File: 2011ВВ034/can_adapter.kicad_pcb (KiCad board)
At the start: 2 copper layers, 31 x 12 mm, 8 parts

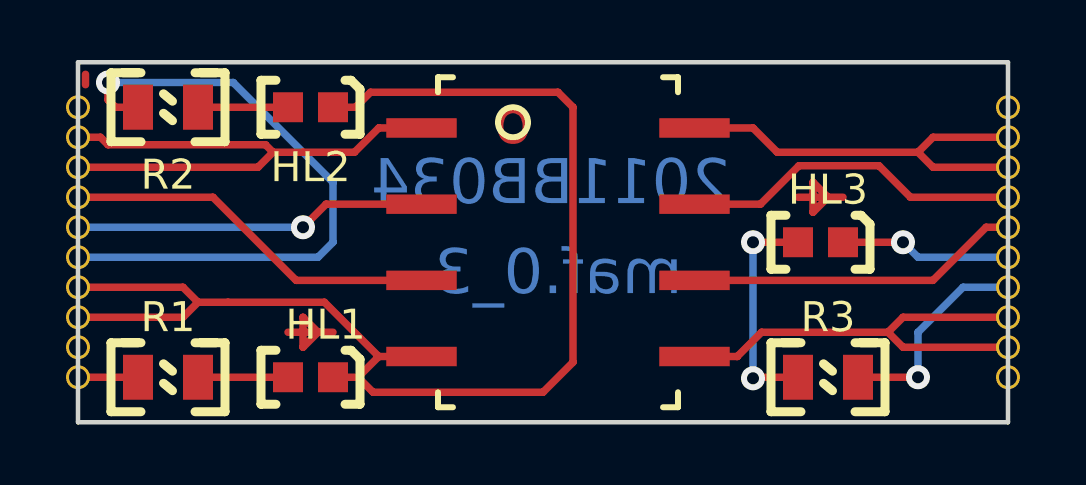
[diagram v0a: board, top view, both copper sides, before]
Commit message: увеличены зазоры и квадратизированы площадки
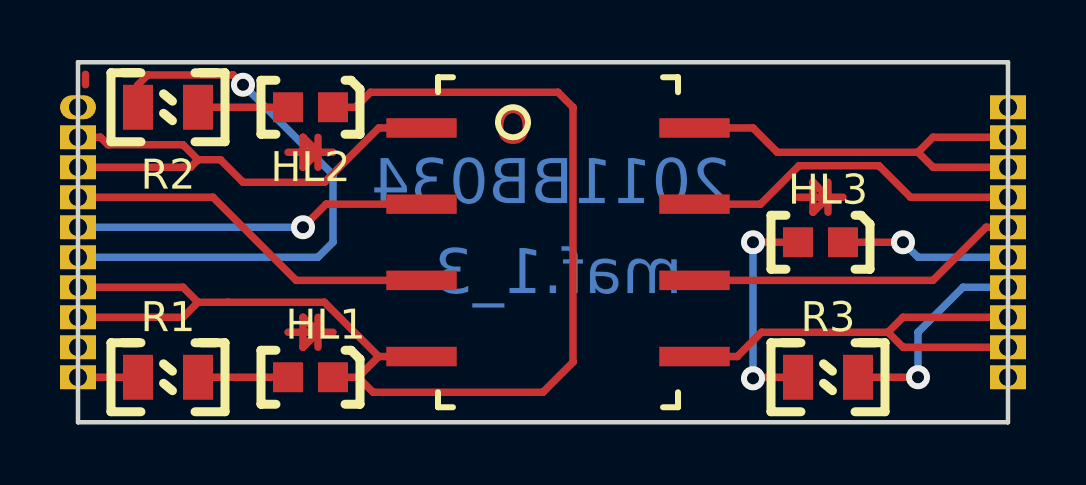
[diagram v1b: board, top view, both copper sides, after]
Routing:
- net (no net): track 8.18 -> 15.1 mm
- net Net-(A1-Pad2A): track 18.7 -> 16.9 mm
- net Net-(A1-Pad6A): track 21.3 -> 19.7 mm
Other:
- board text added: "maf.1_3"
- board text removed: "maf.0_3"
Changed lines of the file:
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@@
     (thickness 1.6)
     (drawings 7)
-    (tracks 96)
+    (tracks 106)
     (zones 0)
     (modules 8)
@@
     (mod_text_size 1 1)
     (mod_text_width 0.15)
-    (pad_size 1.524 1.524)
-    (pad_drill 0.762)
+    (pad_size 1.2 0.8)
+    (pad_drill 0.6)
     (pad_to_mask_clearance 0.05)
     (solder_mask_min_width 0.2)
@@
       (drillshape 0)
       (scaleselection 1)
-      (outputdirectory "maf_3/"))
+      (outputdirectory "maf1_3/"))
   )
   (net 0 "")
@@
       (effects (font (size 2 1.6) (thickness 0.3)))
     )
-    (pad 10B thru_hole circle (at 15.5 -4.5) (size 0.8 0.8) (drill 0.6) (layers *.Cu *.Mask)
+    (pad 10B thru_hole rect (at 15.5 -4.5) (size 1.2 0.8) (drill 0.6) (layers *.Cu *.Mask)
       (net 11 "Net-(A1-Pad10B)"))
-    (pad 9B thru_hole circle (at 15.5 -3.5) (size 0.8 0.8) (drill 0.6) (layers *.Cu *.Mask)
+    (pad 9B thru_hole rect (at 15.5 -3.5) (size 1.2 0.8) (drill 0.6) (layers *.Cu *.Mask)
       (net 10 "Net-(A1-Pad8B)"))
-    (pad 8B thru_hole circle (at 15.5 -2.5) (size 0.8 0.8) (drill 0.6) (layers *.Cu *.Mask)
+    (pad 8B thru_hole rect (at 15.5 -2.5) (size 1.2 0.8) (drill 0.6) (layers *.Cu *.Mask)
       (net 10 "Net-(A1-Pad8B)"))
-    (pad 7B thru_hole circle (at 15.5 -1.5) (size 0.8 0.8) (drill 0.6) (layers *.Cu *.Mask)
+    (pad 7B thru_hole rect (at 15.5 -1.5) (size 1.2 0.8) (drill 0.6) (layers *.Cu *.Mask)
       (net 9 "Net-(A1-Pad7B)"))
-    (pad 6B thru_hole circle (at 15.5 -0.5) (size 0.8 0.8) (drill 0.6) (layers *.Cu *.Mask)
+    (pad 6B thru_hole rect (at 15.5 -0.5) (size 1.2 0.8) (drill 0.6) (layers *.Cu *.Mask)
       (net 8 "Net-(A1-Pad6B)"))
-    (pad 5B thru_hole circle (at 15.5 0.5) (size 0.8 0.8) (drill 0.6) (layers *.Cu *.Mask)
+    (pad 5B thru_hole rect (at 15.5 0.5) (size 1.2 0.8) (drill 0.6) (layers *.Cu *.Mask)
       (net 12 "Net-(A1-Pad5B)"))
-    (pad 4B thru_hole circle (at 15.5 1.5) (size 0.8 0.8) (drill 0.6) (layers *.Cu *.Mask)
+    (pad 4B thru_hole rect (at 15.5 1.5) (size 1.2 0.8) (drill 0.6) (layers *.Cu *.Mask)
       (net 13 "Net-(A1-Pad4B)"))
-    (pad 3B thru_hole circle (at 15.5 2.5) (size 0.8 0.8) (drill 0.6) (layers *.Cu *.Mask)
+    (pad 3B thru_hole rect (at 15.5 2.5) (size 1.2 0.8) (drill 0.6) (layers *.Cu *.Mask)
       (net 7 "Net-(A1-Pad2B)"))
-    (pad 2B thru_hole circle (at 15.5 3.5) (size 0.8 0.8) (drill 0.6) (layers *.Cu *.Mask)
+    (pad 2B thru_hole rect (at 15.5 3.5) (size 1.2 0.8) (drill 0.6) (layers *.Cu *.Mask)
       (net 7 "Net-(A1-Pad2B)"))
-    (pad 10A thru_hole circle (at -15.5 4.5) (size 0.8 0.8) (drill 0.6) (layers *.Cu *.Mask)
+    (pad 10A thru_hole rect (at -15.5 4.5) (size 1.2 0.8) (drill 0.6) (layers *.Cu *.Mask)
       (net 14 "Net-(A1-Pad10A)"))
-    (pad 9A thru_hole circle (at -15.5 3.5) (size 0.8 0.8) (drill 0.6) (layers *.Cu *.Mask)
+    (pad 9A thru_hole rect (at -15.5 3.5) (size 1.2 0.8) (drill 0.6) (layers *.Cu *.Mask)
       (net 15 "Net-(A1-Pad9A)"))
-    (pad 8A thru_hole circle (at -15.5 2.5) (size 0.8 0.8) (drill 0.6) (layers *.Cu *.Mask)
+    (pad 8A thru_hole rect (at -15.5 2.5) (size 1.2 0.8) (drill 0.6) (layers *.Cu *.Mask)
       (net 6 "Net-(A1-Pad7A)"))
-    (pad 7A thru_hole circle (at -15.5 1.5) (size 0.8 0.8) (drill 0.6) (layers *.Cu *.Mask)
+    (pad 7A thru_hole rect (at -15.5 1.5) (size 1.2 0.8) (drill 0.6) (layers *.Cu *.Mask)
       (net 6 "Net-(A1-Pad7A)"))
-    (pad 6A thru_hole circle (at -15.5 0.5) (size 0.8 0.8) (drill 0.6) (layers *.Cu *.Mask)
+    (pad 6A thru_hole rect (at -15.5 0.5) (size 1.2 0.8) (drill 0.6) (layers *.Cu *.Mask)
       (net 16 "Net-(A1-Pad6A)"))
-    (pad 5A thru_hole circle (at -15.5 -0.5) (size 0.8 0.8) (drill 0.6) (layers *.Cu *.Mask)
+    (pad 5A thru_hole rect (at -15.5 -0.5) (size 1.2 0.8) (drill 0.6) (layers *.Cu *.Mask)
       (net 4 "Net-(A1-Pad5A)"))
-    (pad 4A thru_hole circle (at -15.5 -1.5) (size 0.8 0.8) (drill 0.6) (layers *.Cu *.Mask)
+    (pad 4A thru_hole rect (at -15.5 -1.5) (size 1.2 0.8) (drill 0.6) (layers *.Cu *.Mask)
       (net 5 "Net-(A1-Pad4A)"))
-    (pad 3A thru_hole circle (at -15.5 -2.5) (size 0.8 0.8) (drill 0.6) (layers *.Cu *.Mask)
+    (pad 3A thru_hole rect (at -15.5 -2.5) (size 1.2 0.8) (drill 0.6) (layers *.Cu *.Mask)
       (net 2 "Net-(A1-Pad2A)"))
-    (pad 2A thru_hole circle (at -15.5 -3.5) (size 0.8 0.8) (drill 0.6) (layers *.Cu *.Mask)
+    (pad 2A thru_hole rect (at -15.5 -3.5) (size 1.2 0.8) (drill 0.6) (layers *.Cu *.Mask)
       (net 2 "Net-(A1-Pad2A)"))
-    (pad 1B thru_hole circle (at 15.5 4.5) (size 0.8 0.8) (drill 0.6) (layers *.Cu *.Mask)
+    (pad 1B thru_hole rect (at 15.5 4.5) (size 1.2 0.8) (drill 0.6) (layers *.Cu *.Mask)
       (net 3 "Net-(A1-Pad1B)"))
-    (pad 1A thru_hole circle (at -15.5 -4.5) (size 0.8 0.8) (drill 0.6) (layers *.Cu *.Mask)
+    (pad 1A thru_hole oval (at -15.5 -4.5) (size 1.2 0.8) (drill 0.6) (layers *.Cu *.Mask)
       (net 1 "Net-(A1-Pad1A)"))
   )
@@
     (effects (font (size 1.5 1.5) (thickness 0.3)))
   )
-  (gr_text maf.0_3 (at 176.5 55.5) (layer B.Cu)
+  (gr_text maf.1_3 (at 176.5 55.5) (layer B.Cu)
     (effects (font (size 1.5 1.5) (thickness 0.3)) (justify mirror))
   )
@@
   (segment (start 184.500001 53) (end 185.499999 53) (width 0.25) (layer F.Cu) (net 0))
   (segment (start 160.75 49.25) (end 160.75 48.90001) (width 0.25) (layer F.Cu) (net 0))
-  (segment (start 160.5 52) (end 166.5 52) (width 0.25) (layer F.Cu) (net 2))
-  (segment (start 166.5 52) (end 167 51.5) (width 0.25) (layer F.Cu) (net 2))
-  (segment (start 169.715 51.5) (end 168 51.5) (width 0.25) (layer F.Cu) (net 2))
-  (segment (start 170.525 50.69) (end 169.715 51.5) (width 0.25) (layer F.Cu) (net 2))
-  (segment (start 171.95 50.69) (end 170.525 50.69) (width 0.25) (layer F.Cu) (net 2))
-  (segment (start 167 51.5) (end 168 51.5) (width 0.25) (layer F.Cu) (net 2))
-  (segment (start 166.75 51.25) (end 167 51.5) (width 0.25) (layer F.Cu) (net 2))
-  (segment (start 161.25 51) (end 161.5 51.25) (width 0.25) (layer F.Cu) (net 2))
-  (segment (start 160.5 51) (end 161.25 51) (width 0.25) (layer F.Cu) (net 2))
-  (segment (start 166.75 51.25) (end 161.5 51.25) (width 0.25) (layer F.Cu) (net 2))
+  (segment (start 168.5 57) (end 168.5 58) (width 0.25) (layer F.Cu) (net 0))
+  (segment (start 185.5 52.5) (end 185.5 53.5) (width 0.25) (layer F.Cu) (net 0))
+  (segment (start 167.500001 51.5) (end 168.499999 51.5) (width 0.25) (layer F.Cu) (net 0))
+  (segment (start 168.499999 51.5) (end 168 51.999999) (width 0.25) (layer F.Cu) (net 0))
+  (segment (start 168 51.999999) (end 168 51.000001) (width 0.25) (layer F.Cu) (net 0))
+  (segment (start 168 51.000001) (end 168.499999 51.5) (width 0.25) (layer F.Cu) (net 0))
+  (segment (start 168.499999 51.5) (end 169 51.5) (width 0.25) (layer F.Cu) (net 0))
+  (segment (start 168.5 51) (end 168.5 52) (width 0.25) (layer F.Cu) (net 0))
+  (segment (start 161.25 51) (end 160.5 51) (width 0.25) (layer F.Cu) (net 2))
+  (segment (start 161.5 51.25) (end 161.25 51) (width 0.25) (layer F.Cu) (net 2))
+  (segment (start 170.525 50.69) (end 171.95 50.69) (width 0.25) (layer F.Cu) (net 2))
+  (segment (start 168.715 52.5) (end 170.525 50.69) (width 0.25) (layer F.Cu) (net 2))
+  (segment (start 165.25 51.75) (end 166 52.5) (width 0.25) (layer F.Cu) (net 2))
+  (segment (start 166 52.5) (end 168.715 52.5) (width 0.25) (layer F.Cu) (net 2))
+  (segment (start 164 52) (end 164.25 52) (width 0.25) (layer F.Cu) (net 2))
+  (segment (start 160.5 52) (end 164 52) (width 0.25) (layer F.Cu) (net 2))
+  (segment (start 164.25 52) (end 164.5 51.75) (width 0.25) (layer F.Cu) (net 2))
+  (segment (start 164.5 51.75) (end 164 51.25) (width 0.25) (layer F.Cu) (net 2))
+  (segment (start 164 51.25) (end 161.5 51.25) (width 0.25) (layer F.Cu) (net 2))
+  (segment (start 164.5 51.75) (end 165.25 51.75) (width 0.25) (layer F.Cu) (net 2))
   (via (at 168 54) (size 0.8) (drill 0.4) (layers F.Cu B.Cu) (net 4))
   (segment (start 171.95 53.23) (end 168.77 53.23) (width 0.25) (layer F.Cu) (net 4))
@@
   (segment (start 188.5 59) (end 186.5 59) (width 0.25) (layer F.Cu) (net 13))
   (segment (start 162.5 59) (end 160.5 59) (width 0.25) (layer F.Cu) (net 14))
-  (via (at 161.5 49.175) (size 0.8) (drill 0.4) (layers F.Cu B.Cu) (net 16))
-  (segment (start 161.75 50) (end 162.5 50) (width 0.25) (layer F.Cu) (net 16))
-  (segment (start 161.5 49.175) (end 161.5 49.75) (width 0.25) (layer F.Cu) (net 16))
-  (segment (start 161.5 49.75) (end 161.75 50) (width 0.25) (layer F.Cu) (net 16))
-  (segment (start 165.675 49.175) (end 161.5 49.175) (width 0.25) (layer B.Cu) (net 16))
-  (segment (start 169 52.5) (end 165.675 49.175) (width 0.25) (layer B.Cu) (net 16))
-  (segment (start 169 54.5) (end 169 52.5) (width 0.25) (layer B.Cu) (net 16))
+  (via (at 166 49.25) (size 0.8) (drill 0.4) (layers F.Cu B.Cu) (net 16))
+  (segment (start 165.674999 48.924999) (end 166 49.25) (width 0.25) (layer F.Cu) (net 16))
+  (segment (start 162.825001 48.924999) (end 165.674999 48.924999) (width 0.25) (layer F.Cu) (net 16))
+  (segment (start 162.5 49.25) (end 162.825001 48.924999) (width 0.25) (layer F.Cu) (net 16))
+  (segment (start 162.5 50) (end 162.5 49.25) (width 0.25) (layer F.Cu) (net 16))
+  (segment (start 169 52.25) (end 166 49.25) (width 0.25) (layer B.Cu) (net 16))
+  (segment (start 169 54.5) (end 169 52.25) (width 0.25) (layer B.Cu) (net 16))
   (segment (start 168.5 55) (end 169 54.5) (width 0.25) (layer B.Cu) (net 16))
   (segment (start 160.5 55) (end 168.5 55) (width 0.25) (layer B.Cu) (net 16))
